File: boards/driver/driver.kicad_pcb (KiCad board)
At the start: 2 copper layers, 228.6 x 116.8 mm, 485 parts, among them Q1 MMBT2907, Q10 MMBT2907, Q11 MMBT2222, Q12 MMBT2907, Q13 MMBT2222, Q14 MMBT2907, Q15 MMBT2222, Q16 MMBT2907, Q17 MMBT2222, Q18 MMBT2907, Q19 MMBT2222, Q2 MMBT2222, Q20 MMBT2907, Q21 MMBT2222, Q22 MMBT2907, Q23 MMBT2222, Q24 MMBT2907, Q25 MMBT2222, Q26 MMBT2907, Q27 MMBT2222, Q28 MMBT2222, Q29 MMBT2222, Q3 MMBT2222, Q30 MMBT2222, Q31 MMBT2222, Q32 MMBT2222, Q33 MMBT2222, Q34 MMBT2222, Q35 MMBT2222, Q36 MMBT2222, Q37 MMBT2222, Q38 MMBT2222, Q39 MMBT2222, Q4 MMBT2907, Q40 MMBT2222, Q41 MMBT2222, Q42 MMBT2222, Q43 MMBT2222, Q44 MMBT2222, Q45 MMBT2222, Q46 MMBT2222, Q47 MMBT2222, Q48 MMBT2222, Q49 MMBT2222, Q5 MMBT2222, Q50 MMBT2222, Q51 MMBT2222, Q52 MMBT2222, Q53 MMBT2222, Q54 MMBT2222, Q55 MMBT2222, Q56 MMBT2222, Q57 MMBT2222, Q58 MMBT2222, Q59 MMBT2222, Q6 MMBT2907, Q60 MMBT2222, Q61 MMBT2907, Q62 MMBT2222, Q63 MMBT2222, Q64 MMBT2907, Q65 MMBT2222, Q66 MMBT2222, Q67 MMBT2907, Q68 MMBT2222, Q69 MMBT2222, Q7 MMBT2222, Q70 MMBT2222, Q71 MMBT2907, Q72 MMBT2222, Q73 MMBT2222, Q74 MMBT2222, Q75 MMBT2907, Q76 MMBT2222, Q77 MMBT2222, Q78 MMBT2222, Q79 MMBT2907, Q8 MMBT2907, Q80 MMBT2222, Q81 MMBT2222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

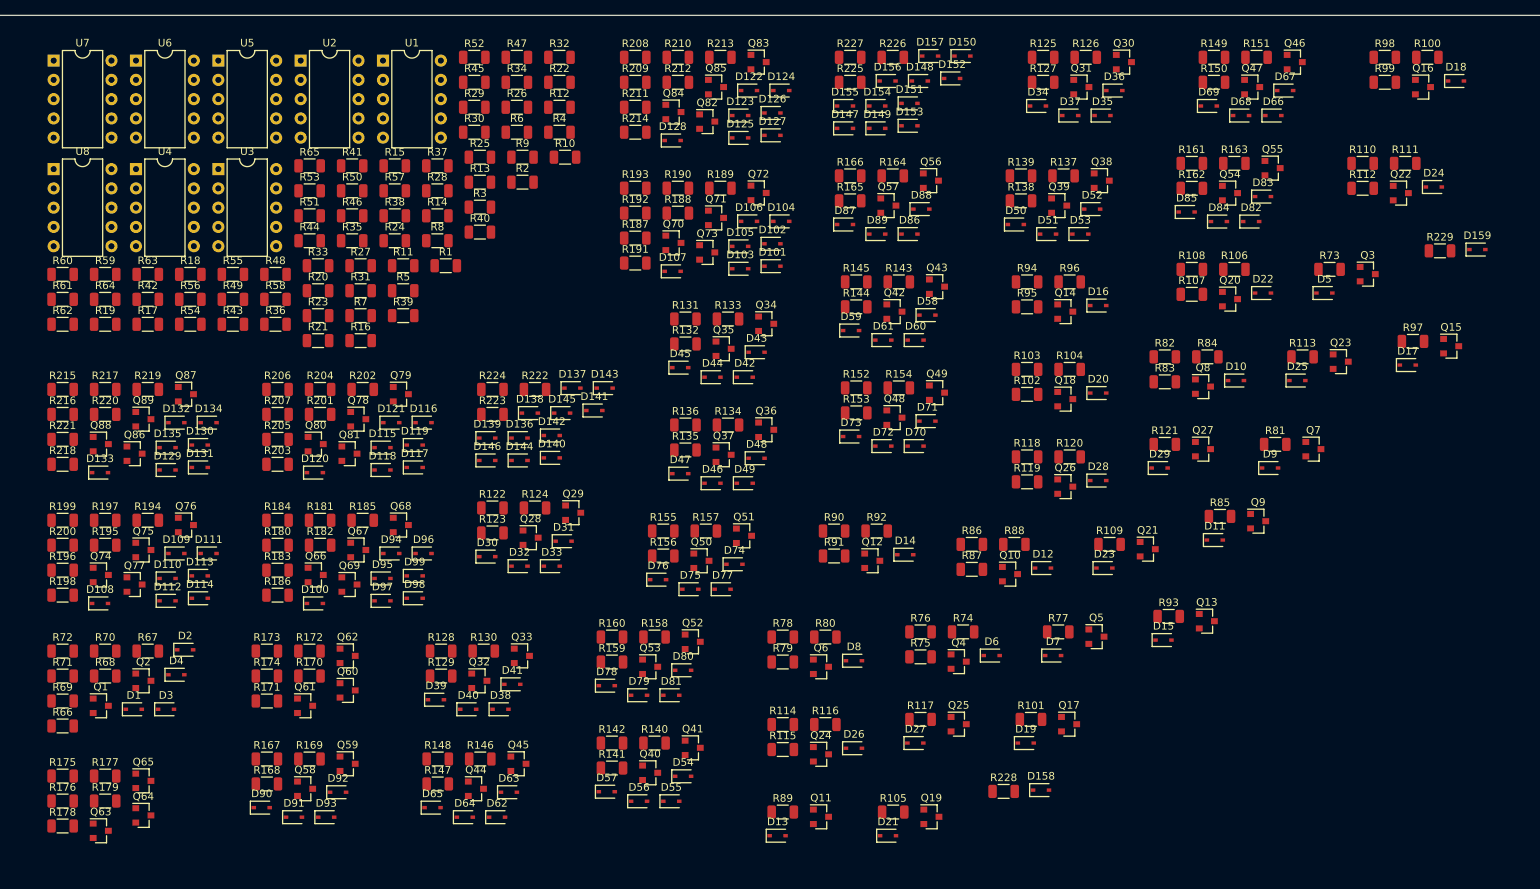
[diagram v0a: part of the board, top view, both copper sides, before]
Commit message: Driver board: a bit more schematic work and some initial footprint selections
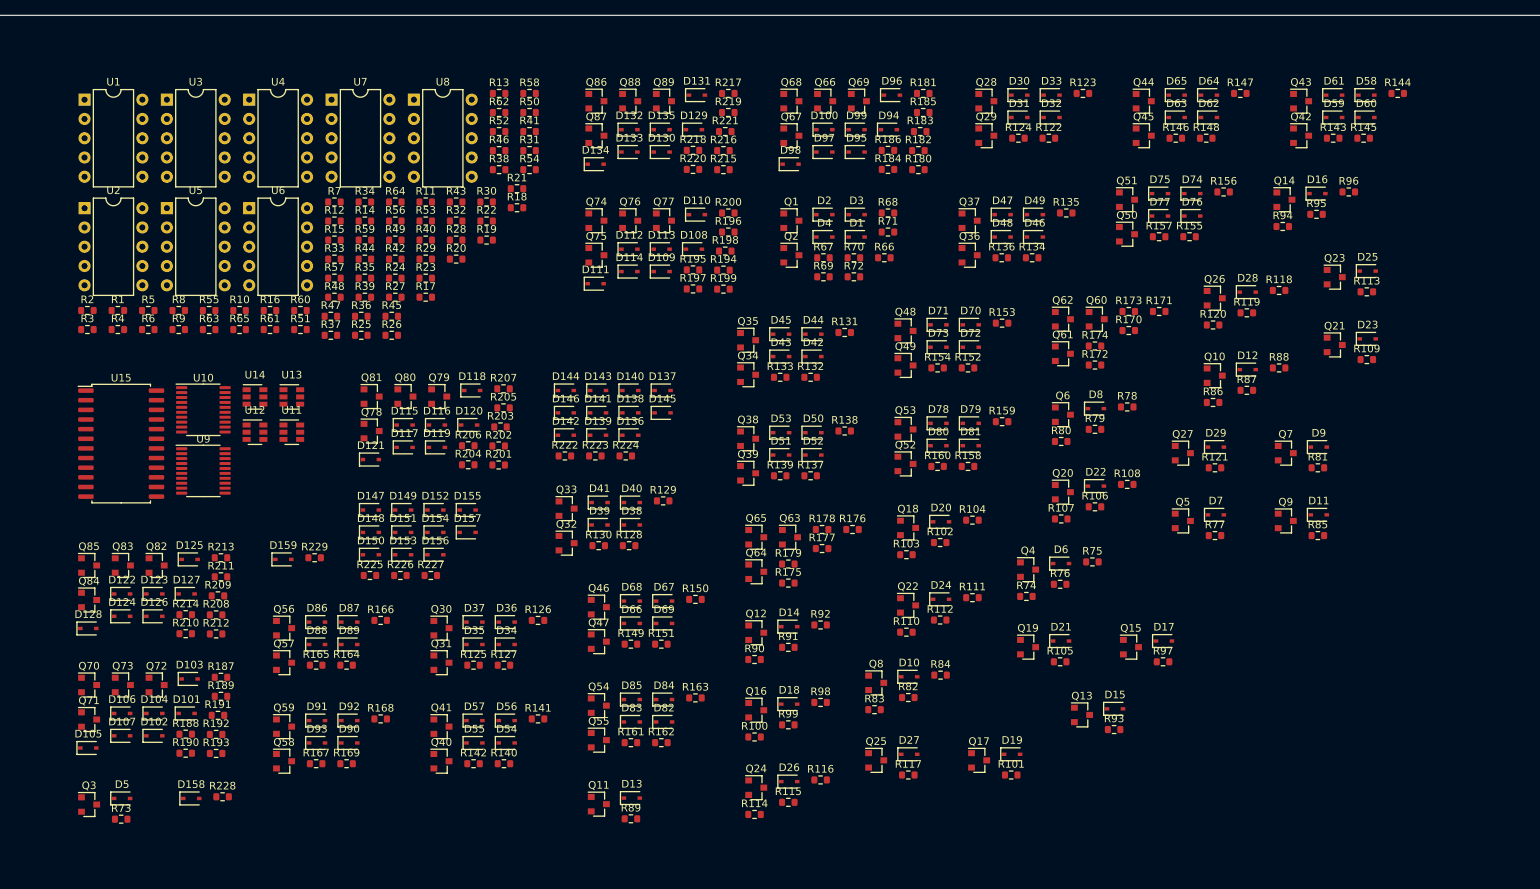
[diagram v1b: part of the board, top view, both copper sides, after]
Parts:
- added U10: 74LVC245, Package_SO:TSSOP-20_4.4x6.5mm_P0.65mm, F.Cu at (71.4, 77.4)
- added U11: 74LVC2G04, Package_TO_SOT_SMD:SOT-23-6, F.Cu at (83.0, 80.3)
- added U12: 74LVC2G04, Package_TO_SOT_SMD:SOT-23-6, F.Cu at (78.2, 80.3)
- added U13: 74LVC2G04, Package_TO_SOT_SMD:SOT-23-6, F.Cu at (83.0, 75.7)
- added U14: 74LVC2G04, Package_TO_SOT_SMD:SOT-23-6, F.Cu at (78.2, 75.7)
- added U15: 74HC4514, Package_SO:SOIC-24W_7.5x15.4mm_P1.27mm, F.Cu at (60.6, 81.8)
- added U9: 74LVC245, Package_SO:TSSOP-20_4.4x6.5mm_P0.65mm, F.Cu at (71.4, 85.4)
- R1, R10, R100, R101, R102, R103, R104, R105, R106, R107, R108, R109, R11, R110, R111, R112, R113, R114, R115, R116, R117, R118, R119, R12, R120, R121, R122, R123, R124, R125, R126, R127, R128, R129, R13, R130, R131, R132, R133, R134, R135, R136, R137, R138, R139, R14, R140, R141, R142, R143, R144, R145, R146, R147, R148, R149, R15, R150, R151, R152, R153, R154, R155, R156, R157, R158, R159, R16, R160, R161, R162, R163, R164, R165, R166, R167, R168, R169, R17, R170, R171, R172, R173, R174, R175, R176, R177, R178, R179, R18, R180, R181, R182, R183, R184, R185, R186, R187, R188, R189, R19, R190, R191, R192, R193, R194, R195, R196, R197, R198, R199, R2, R20, R200, R201, R202, R203, R204, R205, R206, R207, R208, R209, R21, R210, R211, R212, R213, R214, R215, R216, R217, R218, R219, R22, R220, R221, R222, R223, R224, R225, R226, R227, R228, R229, R23, R24, R25, R26, R27, R28, R29, R3, R30, R31, R32, R33, R34, R35, R36, R37, R38, R39, R4, R40, R41, R42, R43, R44, R45, R46, R47, R48, R49, R5, R50, R51, R52, R53, R54, R55, R56, R57, R58, R59, R6, R60, R61, R62, R63, R64, R65, R66, R67, R68, R69, R7, R70, R71, R72, R73, R74, R75, R76, R77, R78, R79, R8, R80, R81, R82, R83, R84, R85, R86, R87, R88, R89, R9, R90, R91, R92, R93, R94, R95, R96, R97, R98, R99: footprint Resistor_SMD:R_1206_3216Metric -> Resistor_SMD:R_0603_1608Metric
- moved Q3 182.4 mm to (56.3, 129.4)
- moved R73 174.9 mm to (60.6, 131.3)
- moved D5 171.9 mm to (60.7, 128.6)
- moved D159 162.6 mm to (81.9, 97.1)
- moved R229 153.7 mm to (86.1, 96.9)
- moved R147 139.5 mm to (208.0, 35.7)
- moved D64 136.6 mm to (203.9, 35.9)
- moved D65 135.8 mm to (199.7, 35.9)
- moved D62 131.5 mm to (203.9, 38.9)
- moved R148 130.2 mm to (203.6, 41.6)
- moved R171 128.3 mm to (197.3, 64.4)
- moved Q44 126.3 mm to (195.3, 36.7)
- moved R100 126.0 mm to (144.0, 120.5)
- moved D63 125.1 mm to (199.7, 38.9)
- moved R66 124.6 mm to (161.1, 57.3)
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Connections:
- R113 pad 2: (no net) -> /FPGA and Power/STEN10
- R117 pad 2: (no net) -> /FPGA and Power/STEN11
- R121 pad 2: (no net) -> /FPGA and Power/STEN12

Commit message: Driver board: finished first rough draft schematic. Lots of placeholders, but at least every place is held.
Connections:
- net /Strand Select/SE01 renamed /Strand Select/SE1
- net /Strand Select/SE02 renamed /Strand Select/SE2
- net /Strand Select/SE03 renamed /Strand Select/SE3
- net /Strand Select/SE04 renamed /Strand Select/SE4
- net /Strand Select/SE05 renamed /Strand Select/SE5
- net /Strand Select/SE06 renamed /Strand Select/SE6
- net /Strand Select/SE07 renamed /Strand Select/SE7
- net /Strand Select/SE08 renamed /Strand Select/SE8
- net /Strand Select/SE09 renamed /Strand Select/SE9
- net /Strand Select/STR01 renamed /Strand Select/STR1
- net /Strand Select/STR02 renamed /Strand Select/STR2
- net /Strand Select/STR03 renamed /Strand Select/STR3
- net /Strand Select/STR04 renamed /Strand Select/STR4
- net /Strand Select/STR05 renamed /Strand Select/STR5
- net /Strand Select/STR06 renamed /Strand Select/STR6
- net /Strand Select/STR07 renamed /Strand Select/STR7
- net /Strand Select/STR08 renamed /Strand Select/STR8
- net /Strand Select/STR09 renamed /Strand Select/STR9
- R101 pad 2: (no net) -> /FPGA and Power/STEN7
- R105 pad 2: (no net) -> /FPGA and Power/STEN8
- R109 pad 2: (no net) -> /FPGA and Power/STEN9
- R122 pad 2: (no net) -> /FPGA and Power/~IL8
- R125 pad 2: (no net) -> /FPGA and Power/~IL7
- R128 pad 2: (no net) -> /FPGA and Power/~IL6
- R131 pad 2: (no net) -> /FPGA and Power/~IL5
- R134 pad 2: (no net) -> /FPGA and Power/~IL4
- R137 pad 2: (no net) -> /FPGA and Power/~IL3
- R140 pad 2: (no net) -> /FPGA and Power/~IL2
- R143 pad 2: (no net) -> /FPGA and Power/~IL1
- R146 pad 2: (no net) -> /FPGA and Power/IL8
- R149 pad 2: (no net) -> /FPGA and Power/IL7
- R152 pad 2: (no net) -> /FPGA and Power/IL6
- R155 pad 2: (no net) -> /FPGA and Power/IL5
- R158 pad 2: (no net) -> /FPGA and Power/IL4
- R161 pad 2: (no net) -> /FPGA and Power/IL3
- R164 pad 2: (no net) -> /FPGA and Power/IL2
- R167 pad 2: (no net) -> /FPGA and Power/IL1
- R77 pad 2: (no net) -> /FPGA and Power/STEN1
- R81 pad 2: (no net) -> /FPGA and Power/STEN2
- R85 pad 2: (no net) -> /FPGA and Power/STEN3
- R89 pad 2: (no net) -> /FPGA and Power/STEN4
- R93 pad 2: (no net) -> /FPGA and Power/STEN5
- R97 pad 2: (no net) -> /FPGA and Power/STEN6
- U11 pad 1: (no net) -> /FPGA and Power/IL1
- U11 pad 3: (no net) -> /FPGA and Power/IL2
- U11 pad 4: (no net) -> /FPGA and Power/~IL2
- U11 pad 6: (no net) -> /FPGA and Power/~IL1
- U12 pad 1: (no net) -> /FPGA and Power/IL3
- U12 pad 3: (no net) -> /FPGA and Power/IL4
- U12 pad 4: (no net) -> /FPGA and Power/~IL4
- U12 pad 6: (no net) -> /FPGA and Power/~IL3
- U13 pad 1: (no net) -> /FPGA and Power/IL5
- U13 pad 3: (no net) -> /FPGA and Power/IL6
- U13 pad 4: (no net) -> /FPGA and Power/~IL6
- U13 pad 6: (no net) -> /FPGA and Power/~IL5
- U14 pad 1: (no net) -> /FPGA and Power/IL7
- U14 pad 3: (no net) -> /FPGA and Power/IL8
- U14 pad 4: (no net) -> /FPGA and Power/~IL8
- U14 pad 6: (no net) -> /FPGA and Power/~IL7
- U15 pad 10: (no net) -> /FPGA and Power/STEN2
- U15 pad 17: (no net) -> /FPGA and Power/STEN9
- U15 pad 18: (no net) -> /FPGA and Power/STEN8
- U15 pad 4: (no net) -> /FPGA and Power/STEN7
- U15 pad 5: (no net) -> /FPGA and Power/STEN6
- U15 pad 6: (no net) -> /FPGA and Power/STEN5
- U15 pad 7: (no net) -> /FPGA and Power/STEN4
- U15 pad 8: (no net) -> /FPGA and Power/STEN3
- U15 pad 9: (no net) -> /FPGA and Power/STEN1

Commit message: Driver board: significant cleanup. Moved sense amp pairs into a subsheet, split tuning resistors into two globally, pushed input circuits into their corresponding sheets.
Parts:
- removed R1, R2: 2.7k, Resistor_SMD:R_0603_1608Metric
- removed U1: SN7524, Package_DIP:DIP-10_W7.62mm
- added C10: 0.1uF, Capacitor_SMD:C_0603_1608Metric, F.Cu at (99.2, 89.6)
- added C11: 0.1uF, Capacitor_SMD:C_0603_1608Metric, F.Cu at (95.2, 94.6)
- added C12: 10nF, Capacitor_SMD:C_0603_1608Metric, F.Cu at (170.0, 43.5)
- added C13: 100pF, Capacitor_SMD:C_0603_1608Metric, F.Cu at (147.3, 64.6)
- added C14: 0.1uF, Capacitor_SMD:C_0603_1608Metric, F.Cu at (166.0, 43.5)
- added C15: 0.1uF, Capacitor_SMD:C_0603_1608Metric, F.Cu at (162.0, 46.0)
- added C16: 10nF, Capacitor_SMD:C_0603_1608Metric, F.Cu at (97.0, 117.4)
- added C17: 100pF, Capacitor_SMD:C_0603_1608Metric, F.Cu at (78.3, 136.0)
- added C18: 0.1uF, Capacitor_SMD:C_0603_1608Metric, F.Cu at (89.0, 124.9)
- added C19: 0.1uF, Capacitor_SMD:C_0603_1608Metric, F.Cu at (93.0, 119.9)
- added C20: 10nF, Capacitor_SMD:C_0603_1608Metric, F.Cu at (51.6, 144.2)
- added C21: 100pF, Capacitor_SMD:C_0603_1608Metric, F.Cu at (47.6, 146.7)
- added C22: 0.1uF, Capacitor_SMD:C_0603_1608Metric, F.Cu at (43.6, 151.8)
- added C23: 0.1uF, Capacitor_SMD:C_0603_1608Metric, F.Cu at (33.0, 162.8)
- added C24: 10nF, Capacitor_SMD:C_0603_1608Metric, F.Cu at (215.4, 19.1)
- added C25: 100pF, Capacitor_SMD:C_0603_1608Metric, F.Cu at (211.3, 21.7)
- added C26: 0.1uF, Capacitor_SMD:C_0603_1608Metric, F.Cu at (207.3, 26.7)
- added C27: 0.1uF, Capacitor_SMD:C_0603_1608Metric, F.Cu at (192.7, 37.7)
- added C28: 10nF, Capacitor_SMD:C_0603_1608Metric, F.Cu at (140.6, 94.6)
- added C29: 100pF, Capacitor_SMD:C_0603_1608Metric, F.Cu at (140.6, 87.1)
- added C3: 6.8uF, Capacitor_Tantalum_SMD:CP_EIA-7343-31_Kemet-D, F.Cu at (208.3, 94.6)
- added C30: 0.1uF, Capacitor_SMD:C_0603_1608Metric, F.Cu at (140.6, 89.6)
- added C31: 0.1uF, Capacitor_SMD:C_0603_1608Metric, F.Cu at (140.6, 84.6)
- added C32: 10nF, Capacitor_SMD:C_0603_1608Metric, F.Cu at (162.0, 16.6)
- added C33: 100pF, Capacitor_SMD:C_0603_1608Metric, F.Cu at (147.3, 37.7)
- added C34: 0.1uF, Capacitor_SMD:C_0603_1608Metric, F.Cu at (166.0, 16.6)
- added C35: 0.1uF, Capacitor_SMD:C_0603_1608Metric, F.Cu at (162.0, 19.1)
- added C36: 6.8uF, Capacitor_Tantalum_SMD:CP_EIA-7343-31_Kemet-D, F.Cu at (186.4, 108.2)
- added C37: 6.8uF, Capacitor_Tantalum_SMD:CP_EIA-7343-31_Kemet-D, F.Cu at (206.4, 108.2)
- added C38: 6.8uF, Capacitor_Tantalum_SMD:CP_EIA-7343-31_Kemet-D, F.Cu at (259.2, 31.9)
- added C39: 6.8uF, Capacitor_Tantalum_SMD:CP_EIA-7343-31_Kemet-D, F.Cu at (162.3, 140.3)
- added C4: 10nF, Capacitor_SMD:C_0603_1608Metric, F.Cu at (47.6, 114.9)
- added C40: 6.8uF, Capacitor_Tantalum_SMD:CP_EIA-7343-31_Kemet-D, F.Cu at (160.7, 153.9)
- added C41: 6.8uF, Capacitor_Tantalum_SMD:CP_EIA-7343-31_Kemet-D, F.Cu at (230.1, 76.1)
- added C42: 6.8uF, Capacitor_Tantalum_SMD:CP_EIA-7343-31_Kemet-D, F.Cu at (184.2, 120.8)
- added C43: 6.8uF, Capacitor_Tantalum_SMD:CP_EIA-7343-31_Kemet-D, F.Cu at (259.2, 44.5)
- added C44: 6.8uF, Capacitor_Tantalum_SMD:CP_EIA-7343-31_Kemet-D, F.Cu at (235.3, 63.5)
- added C45: 1.0uF, Capacitor_Tantalum_SMD:CP_EIA-3216-18_Kemet-A, F.Cu at (158.3, 70.6)
- added C46: 1.0uF, Capacitor_Tantalum_SMD:CP_EIA-3216-18_Kemet-A, F.Cu at (63.4, 160.0)
- added C47: 0.1uF, Capacitor_SMD:C_0603_1608Metric, F.Cu at (41.0, 50.1)
- added C48: 0.1uF, Capacitor_SMD:C_0603_1608Metric, F.Cu at (30.4, 64.8)
- added C49: 0.33uF, Capacitor_SMD:C_0603_1608Metric, F.Cu at (26.4, 64.8)
- added C5: 100pF, Capacitor_SMD:C_0603_1608Metric, F.Cu at (43.6, 117.4)
- added C50: 10nF, Capacitor_SMD:C_0603_1608Metric, F.Cu at (34.4, 62.3)
- added C51: 0.1uF, Capacitor_SMD:C_0603_1608Metric, F.Cu at (34.4, 59.8)
- added C52: 0.1uF, Capacitor_SMD:C_0603_1608Metric, F.Cu at (26.4, 59.8)
- added C53: 0.1uF, Capacitor_SMD:C_0603_1608Metric, F.Cu at (41.0, 52.6)
- added C54: 0.1uF, Capacitor_SMD:C_0603_1608Metric, F.Cu at (26.4, 67.3)
- added C55: 0.1uF, Capacitor_SMD:C_0603_1608Metric, F.Cu at (30.4, 59.8)
- added C6: 0.1uF, Capacitor_SMD:C_0603_1608Metric, F.Cu at (29.0, 136.0)
- added C7: 0.1uF, Capacitor_SMD:C_0603_1608Metric, F.Cu at (43.6, 114.9)
- added C8: 10nF, Capacitor_SMD:C_0603_1608Metric, F.Cu at (84.6, 105.7)
- added C9: 100pF, Capacitor_SMD:C_0603_1608Metric, F.Cu at (103.2, 87.1)
- added J1: Barrel_Jack_Switch, Connector_BarrelJack:BarrelJack_Horizontal, F.Cu at (68.2, 20.7)
- added J2: Conn_01x24, Connector_PinSocket_2.54mm:PinSocket_1x24_P2.54mm_Vertical, F.Cu at (17.5, 17.7)
- added J3: Conn_02x06_Top_Bottom, Connector_PinSocket_2.54mm:PinSocket_2x06_P2.54mm_Vertical, F.Cu at (51.3, 17.7)
- added J4: Conn_01x24, Connector_PinSocket_2.54mm:PinSocket_1x24_P2.54mm_Vertical, F.Cu at (22.1, 17.7)
- added J5: Conn_01x24, Connector_PinHeader_1.00mm:PinHeader_1x24_P1.00mm_Vertical, F.Cu at (16.9, 84.8)
- added J6: Conn_01x24, Connector_PinHeader_1.00mm:PinHeader_1x24_P1.00mm_Vertical, F.Cu at (20.2, 84.8)
- added J7: Conn_01x24, Connector_PinHeader_1.00mm:PinHeader_1x24_P1.00mm_Vertical, F.Cu at (23.6, 84.8)
- added J8: Conn_01x24, Connector_PinHeader_1.00mm:PinHeader_1x24_P1.00mm_Vertical, F.Cu at (26.9, 84.8)
- added L1: 8.2uH, Inductor_SMD:L_1812_4532Metric, F.Cu at (216.7, 94.2)
- added L10: 2.2uH, Inductor_SMD:L_1812_4532Metric, F.Cu at (235.9, 35.8)
- added L11: 2.2uH, Inductor_SMD:L_1812_4532Metric, F.Cu at (184.9, 80.6)
- added L12: 2.2uH, Inductor_SMD:L_1812_4532Metric, F.Cu at (212.0, 59.4)
- added L13: 2.2uH, Inductor_SMD:L_1812_4532Metric, F.Cu at (138.9, 126.2)
- added L14: 2.2uH, Inductor_SMD:L_1812_4532Metric, F.Cu at (160.8, 112.6)
- added L15: 2.2uH, Inductor_SMD:L_1812_4532Metric, F.Cu at (115.5, 148.5)
- added L16: 2.2uH, Inductor_SMD:L_1812_4532Metric, F.Cu at (257.3, 17.9)
- added L17: 2.2uH, Inductor_SMD:L_1812_4532Metric, F.Cu at (93.6, 148.5)
- added L18: 2.2uH, Inductor_SMD:L_1812_4532Metric, F.Cu at (138.9, 112.6)
- added L19: 3.9uH, Inductor_SMD:L_1812_4532Metric, F.Cu at (64.0, 142.9)
- added L2: 8.2uH, Inductor_SMD:L_1812_4532Metric, F.Cu at (194.8, 107.8)
- added L20: 3.9uH, Inductor_SMD:L_1812_4532Metric, F.Cu at (64.0, 147.9)
- added L21: 3.9uH, Inductor_SMD:L_1812_4532Metric, F.Cu at (182.4, 49.6)
- added L22: 3.9uH, Inductor_SMD:L_1812_4532Metric, F.Cu at (182.4, 44.7)
- added L23: 3.9uH, Inductor_SMD:L_1812_4532Metric, F.Cu at (109.4, 112.6)
- added L24: 3.9uH, Inductor_SMD:L_1812_4532Metric, F.Cu at (109.4, 117.5)
- added L25: 3.9uH, Inductor_SMD:L_1812_4532Metric, F.Cu at (227.7, 17.9)
- added L26: 3.9uH, Inductor_SMD:L_1812_4532Metric, F.Cu at (227.7, 22.8)
- added L27: 3.9uH, Inductor_SMD:L_1812_4532Metric, F.Cu at (109.4, 130.5)
- added L28: 3.9uH, Inductor_SMD:L_1812_4532Metric, F.Cu at (109.4, 135.5)
- added L29: 3.9uH, Inductor_SMD:L_1812_4532Metric, F.Cu at (182.4, 62.6)
- added L3: 2.2uH, Inductor_SMD:L_1812_4532Metric, F.Cu at (184.9, 94.2)
- added L30: 3.9uH, Inductor_SMD:L_1812_4532Metric, F.Cu at (182.4, 67.6)
- added L31: 8.2uH, Inductor_SMD:L_1812_4532Metric, F.Cu at (214.8, 107.8)
- added L32: 8.2uH, Inductor_SMD:L_1812_4532Metric, F.Cu at (267.6, 31.5)
- added L33: 8.2uH, Inductor_SMD:L_1812_4532Metric, F.Cu at (170.7, 139.8)
- added L34: 8.2uH, Inductor_SMD:L_1812_4532Metric, F.Cu at (169.1, 153.4)
- added L35: 8.2uH, Inductor_SMD:L_1812_4532Metric, F.Cu at (238.5, 75.6)
- added L36: 8.2uH, Inductor_SMD:L_1812_4532Metric, F.Cu at (192.6, 120.4)
- added L37: 8.2uH, Inductor_SMD:L_1812_4532Metric, F.Cu at (267.6, 44.1)
- added L38: 8.2uH, Inductor_SMD:L_1812_4532Metric, F.Cu at (243.7, 63.0)
- added L4: 2.2uH, Inductor_SMD:L_1812_4532Metric, F.Cu at (137.3, 153.4)
- added L5: 2.2uH, Inductor_SMD:L_1812_4532Metric, F.Cu at (160.8, 126.2)
- added L6: 2.2uH, Inductor_SMD:L_1812_4532Metric, F.Cu at (206.8, 80.6)
- added L7: 2.2uH, Inductor_SMD:L_1812_4532Metric, F.Cu at (235.9, 49.4)
- added L8: 2.2uH, Inductor_SMD:L_1812_4532Metric, F.Cu at (138.9, 139.8)
- added L9: 2.2uH, Inductor_SMD:L_1812_4532Metric, F.Cu at (137.1, 71.5)
- added Q90: IRF7413, Package_SO:SO-8_3.9x4.9mm_P1.27mm, F.Cu at (59.5, 39.3)
- added R230: NOM, Resistor_SMD:R_0603_1608Metric, F.Cu at (247.5, 24.6)
- added R231: 7.5, Resistor_SMD:R_0603_1608Metric, F.Cu at (235.0, 28.7)
- added R232: NOM, Resistor_SMD:R_0603_1608Metric, F.Cu at (246.4, 19.6)
- added R233: 1k, Resistor_SMD:R_0603_1608Metric, F.Cu at (116.6, 141.4)
- added R234: 1k, Resistor_SMD:R_0603_1608Metric, F.Cu at (128.0, 132.3)
- added R235: 5.1k, Resistor_SMD:R_0603_1608Metric, F.Cu at (128.9, 140.2)
- added R236: 5.1k, Resistor_SMD:R_0603_1608Metric, F.Cu at (129.1, 137.3)
- added R237: 27, Resistor_SMD:R_0603_1608Metric, F.Cu at (124.9, 140.2)
- added R238: 7.5, Resistor_SMD:R_0603_1608Metric, F.Cu at (129.1, 134.8)
- added R239: NOM, Resistor_SMD:R_0603_1608Metric, F.Cu at (125.1, 137.7)
- added R240: 7.5, Resistor_SMD:R_0603_1608Metric, F.Cu at (125.1, 135.2)
- added R241: NOM, Resistor_SMD:R_0603_1608Metric, F.Cu at (120.9, 139.8)
- added R242: 1k, Resistor_SMD:R_0603_1608Metric, F.Cu at (198.1, 67.3)
- added R243: 1k, Resistor_SMD:R_0603_1608Metric, F.Cu at (198.1, 69.8)
- added R244: 5.1k, Resistor_SMD:R_0603_1608Metric, F.Cu at (202.1, 66.9)
- added R245: 5.1k, Resistor_SMD:R_0603_1608Metric, F.Cu at (202.1, 69.4)
- added R246: 27, Resistor_SMD:R_0603_1608Metric, F.Cu at (201.9, 72.3)
- added R247: 7.5, Resistor_SMD:R_0603_1608Metric, F.Cu at (189.6, 73.4)
- added R248: NOM, Resistor_SMD:R_0603_1608Metric, F.Cu at (197.9, 72.3)
- added R249: 7.5, Resistor_SMD:R_0603_1608Metric, F.Cu at (193.9, 71.8)
- added R250: NOM, Resistor_SMD:R_0603_1608Metric, F.Cu at (201.0, 64.3)
- added R251: 200, Resistor_SMD:R_0603_1608Metric, F.Cu at (210.5, 52.3)
- added R252: 200, Resistor_SMD:R_0603_1608Metric, F.Cu at (214.5, 52.3)
- added R253: 200, Resistor_SMD:R_0603_1608Metric, F.Cu at (218.5, 52.3)
- added R254: 200, Resistor_SMD:R_0603_1608Metric, F.Cu at (159.5, 103.0)
- added R255: 200, Resistor_SMD:R_0603_1608Metric, F.Cu at (163.5, 103.0)
- added R256: 200, Resistor_SMD:R_0603_1608Metric, F.Cu at (167.5, 103.0)
- added R257: 3k, Resistor_SMD:R_0603_1608Metric, F.Cu at (157.5, 73.4)
- added R258: 3k, Resistor_SMD:R_0603_1608Metric, F.Cu at (62.6, 162.8)
- added R259: 1020k, Resistor_SMD:R_0603_1608Metric, F.Cu at (26.4, 55.1)
- added R260: 2.87k, Resistor_SMD:R_0603_1608Metric, F.Cu at (30.4, 54.8)
- added R261: 9.76k, Resistor_SMD:R_0603_1608Metric, F.Cu at (34.4, 54.8)
- added R262: 54.9k, Resistor_SMD:R_0603_1608Metric, F.Cu at (30.4, 57.3)
- added R263: 0.025, Resistor_SMD:R_0603_1608Metric, F.Cu at (34.4, 57.3)
- added R264: 10, Resistor_SMD:R_0603_1608Metric, F.Cu at (38.5, 55.1)
- added R265: 1k, Resistor_SMD:R_0603_1608Metric, F.Cu at (38.5, 57.7)
- added R266: 10k, Resistor_SMD:R_0603_1608Metric, F.Cu at (26.4, 62.3)
- added R267: 10k, Resistor_SMD:R_0603_1608Metric, F.Cu at (30.4, 62.3)
- added T1: 1:1, lachesis:Transformer_Murata_786J, F.Cu at (34.3, 129.5)
- added T10: 1:1, lachesis:Transformer_Murata_786J, F.Cu at (34.3, 145.7)
- added T11: 1:1, lachesis:Transformer_Murata_786J, F.Cu at (198.0, 20.7)
- added T12: 1:1, lachesis:Transformer_Murata_786J, F.Cu at (198.0, 31.2)
- added T13: 1:1, lachesis:Transformer_Murata_786J, F.Cu at (131.2, 99.1)
- added T14: 1:1, lachesis:Transformer_Murata_786J, F.Cu at (131.2, 88.6)
- added T15: 1:1, lachesis:Transformer_Murata_786J, F.Cu at (152.7, 31.2)
- added T16: 1:1, lachesis:Transformer_Murata_786J, F.Cu at (152.7, 20.7)
- added T2: 1:1, lachesis:Transformer_Murata_786J, F.Cu at (34.3, 118.9)
- added T3: 1:1, lachesis:Transformer_Murata_786J, F.Cu at (85.9, 99.1)
- added T4: 1:1, lachesis:Transformer_Murata_786J, F.Cu at (85.9, 88.6)
- added T5: 1:1, lachesis:Transformer_Murata_786J, F.Cu at (152.7, 47.5)
- added T6: 1:1, lachesis:Transformer_Murata_786J, F.Cu at (152.7, 58.0)
- added T7: 1:1, lachesis:Transformer_Murata_786J, F.Cu at (79.6, 118.9)
- added T8: 1:1, lachesis:Transformer_Murata_786J, F.Cu at (79.6, 129.5)
- added T9: 1:1, lachesis:Transformer_Murata_786J, F.Cu at (34.3, 156.3)
- added U16: 74LVC2G04, Package_TO_SOT_SMD:SOT-23-6, F.Cu at (31.7, 51.2)
- added U17: 74LVC2G04, Package_TO_SOT_SMD:SOT-23-6, F.Cu at (26.8, 51.2)
- added U18: 74LVC2G04, Package_TO_SOT_SMD:SOT-23-6, F.Cu at (36.5, 51.2)
- Q1, Q10, Q12, Q14, Q16, Q18, Q20, Q22, Q24, Q26, Q4, Q6, Q8: value MMBT2907 -> MMBT2222
- Q11, Q13, Q15, Q17, Q19, Q2, Q21, Q23, Q25, Q27, Q5, Q7, Q9: value MMBT2222 -> MMBT2907
- R10, R15, R16, R33, R34, R39, R40, R41, R42, R47, R48, R7, R8, R9: value 2.7k -> 470
- R100, R104, R108, R112, R116, R120, R76, R80, R84, R88, R92, R96: value 3k -> 5.1k
- R101, R105, R109, R113, R117, R121, R194, R77, R81, R85, R89, R93, R97: value 500 -> 2k
- R102, R106, R110, R114, R118, R78, R82, R86, R90, R94, R98: value 5.1k -> 3k
- R103, R107, R111, R115, R119, R179, R75, R79, R83, R87, R91, R95, R99: value 2k -> 1k
- R122: value 500 -> 3k
- R123, R135, R147, R159: value 390 -> 1k
- R124, R136, R148, R160: value NOM -> 390
- R125, R137, R149, R161: value 500 -> 3.9
- R126, R138, R150, R162: value 390 -> NOM
- R127, R139, R151, R163, R192, R206, R207: value NOM -> 1k
- R128, R140, R152, R164, R180: value 500 -> 390
- R129, R141, R153, R165: value 390 -> 3.9
- R131, R143, R155, R167, R187, R215: value 500 -> 1k
- R133, R145, R157, R169, R185: value NOM -> 3.9
- R134, R146, R158: value 500 -> NOM
- R170: value 1k -> NOM
- R171: value 470 -> 1k
- R172: value 2k -> 390
- R173: value 750 -> 3.9
- R174: value 2k -> NOM
- R176: value 470 -> 390
- R177: value 2k -> 3.9
- R178: value 750 -> NOM
- R181: value 1k -> 3.9
- R182, R203, R74: value 5.1k -> NOM
- R183, R197, R67: value 5.1k -> 1k
- R184: value 27 -> 390
- R188: value 1k -> 470
- R189, R196: value 5.1k -> 2k
- R19, R20, R21, R22, R27, R28, R29, R30, R51, R52, R53, R54, R59, R60, R61, R62: value 470 -> 2.7k
- R190: value 5.1k -> 750
- R191: value 27 -> 2k
- R193: value NOM -> 470
- R195: value 1k -> 750
- R198: value 27 -> 1k
- R199, R200, R71: value NOM -> 5.1k
- R201: value 500 -> 27
- R202: value 1k -> 7.5
- R204, R211: value 5.1k -> 7.5
- R205, R212: value 27 -> NOM
- R208: value 500 -> 5.1k
- R209: value 1k -> 5.1k
- R210: value 5.1k -> 27
- R213, R220: value NOM -> 7.5
- R222: value 200 -> 7.5
- R223: value 200 -> NOM
- R224, R225: value 200 -> 1k
- R226, R227: value 200 -> 5.1k
- R228: value 3k -> 27
- R229: value 3k -> 7.5
- R65: value 5k -> 470
- R66: value 5.1k -> 470
- R68: value 680 -> 5.1k
- R70: value 3k -> 680
- R72: value 6 -> 3k
- R73: value 500 -> 8.2
- U11: value 74LVC2G04 -> 74LVC245; footprint Package_TO_SOT_SMD:SOT-23-6 -> Package_SO:TSSOP-20_4.4x6.5mm_P0.65mm
- U12: value 74LVC2G04 -> JTE0624D05; footprint Package_TO_SOT_SMD:SOT-23-6 -> Converter_DCDC:Converter_DCDC_XP_POWER_JTExxxxDxx_THT
- U13: value 74LVC2G04 -> LTC4231-1; footprint Package_TO_SOT_SMD:SOT-23-6 -> Package_SO:MSOP-12_3x4mm_P0.65mm
- U14: value 74LVC2G04 -> 74HC4514; footprint Package_TO_SOT_SMD:SOT-23-6 -> Package_SO:SOIC-24W_7.5x15.4mm_P1.27mm
- U15: value 74HC4514 -> 74LVC2G04; footprint Package_SO:SOIC-24W_7.5x15.4mm_P1.27mm -> Package_TO_SOT_SMD:SOT-23-6
- U2, U3, U4, U5, U6, U7, U8: footprint Package_DIP:DIP-10_W7.62mm -> Package_DIP:DIP-16_W7.62mm_Socket
- U9: value 74LVC245 -> SN7524; footprint Package_SO:TSSOP-20_4.4x6.5mm_P0.65mm -> Package_DIP:DIP-16_W7.62mm_Socket
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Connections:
- D1 pad 1: Net-(D1-Pad1) -> GND
- D1 pad 2: /Strand Select/BPLSWZ -> Net-(D1-Pad2)
- D10 pad 1: Net-(D10-Pad1) -> GND
- D10 pad 2: /Strand Select/BPLSWZ -> Net-(D10-Pad2)
- D11 pad 1: GND -> Net-(D11-Pad1)
- D11 pad 2: Net-(D11-Pad2) -> /Strand Select/BPLSWZ
- D12 pad 1: Net-(D12-Pad1) -> GND
- D12 pad 2: /Strand Select/BPLSWZ -> Net-(D12-Pad2)
- D13 pad 1: GND -> Net-(D13-Pad1)
- D13 pad 2: Net-(D13-Pad2) -> /Strand Select/BPLSWZ
- D136 pad 1: (no net) -> /Connector/RFD1
- D137 pad 1: (no net) -> /Connector/RFD3
- D138 pad 1: /Rope Drivers/RSTRD4 -> /Connector/RSTRD4
- D139 pad 1: (no net) -> /Connector/RCD1
- D14 pad 1: Net-(D14-Pad1) -> GND
- D14 pad 2: /Strand Select/BPLSWZ -> Net-(D14-Pad2)
- D140 pad 1: (no net) -> /Connector/RCD3
- D141 pad 1: (no net) -> /Connector/RFD2
- D142 pad 1: (no net) -> /Connector/RFD4
- D143 pad 1: /Rope Drivers/RSTRD3 -> /Connector/RSTRD3
- D144 pad 1: (no net) -> /Connector/RCD2
- D145 pad 1: (no net) -> /Connector/RCD4
- D146 pad 1: /Rope Drivers/SETRN1 -> /Connector/SETRN1
- D147 pad 1: (no net) -> /Connector/RFD5
- D148 pad 1: (no net) -> /Connector/RFD7
- D149 pad 1: /Rope Drivers/RSTRD2 -> /Connector/RSTRD2
- D15 pad 1: GND -> Net-(D15-Pad1)
- D15 pad 2: Net-(D15-Pad2) -> /Strand Select/BPLSWZ
- D150 pad 1: (no net) -> /Connector/RCD5
- D151 pad 1: (no net) -> /Connector/RCD7
- D152 pad 1: (no net) -> /Connector/RFD6
- D153 pad 1: (no net) -> /Connector/RFD8
- D154 pad 1: /Rope Drivers/RSTRD1 -> /Connector/RSTRD1
- D155 pad 1: (no net) -> /Connector/RCD6
- D156 pad 1: (no net) -> /Connector/RCD8
- D157 pad 1: /Rope Drivers/SETRN2 -> /Connector/SETRN2
- D16 pad 1: Net-(D16-Pad1) -> GND
- D16 pad 2: /Strand Select/BPLSWZ -> Net-(D16-Pad2)
- D17 pad 1: GND -> Net-(D17-Pad1)
- D17 pad 2: Net-(D17-Pad2) -> /Strand Select/BPLSWZ
- D18 pad 1: Net-(D18-Pad1) -> GND
- D18 pad 2: /Strand Select/BPLSWZ -> Net-(D18-Pad2)
- D19 pad 1: GND -> Net-(D19-Pad1)
- D19 pad 2: Net-(D19-Pad2) -> /Strand Select/BPLSWZ
- D2 pad 2: Net-(D2-Pad2) -> /Strand Select/BPLSWZ
- D20 pad 1: Net-(D20-Pad1) -> GND
- D20 pad 2: /Strand Select/BPLSWZ -> Net-(D20-Pad2)
- D21 pad 1: GND -> Net-(D21-Pad1)
- D21 pad 2: Net-(D21-Pad2) -> /Strand Select/BPLSWZ
- D22 pad 1: Net-(D22-Pad1) -> GND
- D22 pad 2: /Strand Select/BPLSWZ -> Net-(D22-Pad2)
- D23 pad 1: GND -> Net-(D23-Pad1)
- D23 pad 2: Net-(D23-Pad2) -> /Strand Select/BPLSWZ
- D24 pad 1: Net-(D24-Pad1) -> GND
- D24 pad 2: /Strand Select/BPLSWZ -> Net-(D24-Pad2)
- D25 pad 1: GND -> Net-(D25-Pad1)
- D25 pad 2: Net-(D25-Pad2) -> /Strand Select/BPLSWZ
- D26 pad 1: Net-(D26-Pad1) -> GND
- D26 pad 2: /Strand Select/BPLSWZ -> Net-(D26-Pad2)
- D27 pad 1: GND -> Net-(D27-Pad1)
- D27 pad 2: Net-(D27-Pad2) -> /Strand Select/BPLSWZ
- D28 pad 1: Net-(D28-Pad1) -> GND
- D28 pad 2: /Strand Select/BPLSWZ -> Net-(D28-Pad2)
- D29 pad 1: GND -> Net-(D29-Pad1)
- D29 pad 2: Net-(D29-Pad2) -> /Strand Select/BPLSWZ
- D3 pad 2: Net-(D2-Pad1) -> Net-(D3-Pad2)
- D5 pad 2: Net-(D5-Pad2) -> Net-(D4-Pad1)
- D6 pad 1: Net-(D6-Pad1) -> GND
- D6 pad 2: /Strand Select/BPLSWZ -> Net-(D6-Pad2)
- D7 pad 1: GND -> Net-(D7-Pad1)
- D7 pad 2: Net-(D7-Pad2) -> /Strand Select/BPLSWZ
- D8 pad 1: Net-(D8-Pad1) -> GND
- D8 pad 2: /Strand Select/BPLSWZ -> Net-(D8-Pad2)
- D9 pad 1: GND -> Net-(D9-Pad1)
- D9 pad 2: Net-(D9-Pad2) -> /Strand Select/BPLSWZ
- Q1 pad 2: Net-(D1-Pad1) -> Net-(D1-Pad2)
- Q1 pad 3: Net-(Q1-Pad3) -> /Strand Select/RPR
- Q10 pad 2: Net-(D12-Pad1) -> Net-(D12-Pad2)
- Q10 pad 3: /Strand Select/STR4 -> Net-(Q10-Pad3)
- Q11 pad 2: Net-(D13-Pad2) -> Net-(D13-Pad1)
- Q11 pad 3: /Strand Select/SE4 -> /Connector/STR4
- Q12 pad 2: Net-(D14-Pad1) -> Net-(D14-Pad2)
- Q12 pad 3: /Strand Select/STR5 -> Net-(Q12-Pad3)
- Q13 pad 2: Net-(D15-Pad2) -> Net-(D15-Pad1)
- Q13 pad 3: /Strand Select/SE5 -> /Connector/STR5
- Q14 pad 2: Net-(D16-Pad1) -> Net-(D16-Pad2)
- Q14 pad 3: /Strand Select/STR6 -> Net-(Q14-Pad3)
- Q15 pad 2: Net-(D17-Pad2) -> Net-(D17-Pad1)
- Q15 pad 3: /Strand Select/SE6 -> /Connector/STR6
- Q16 pad 2: Net-(D18-Pad1) -> Net-(D18-Pad2)
- Q16 pad 3: /Strand Select/STR7 -> Net-(Q16-Pad3)
- Q17 pad 2: Net-(D19-Pad2) -> Net-(D19-Pad1)
- Q17 pad 3: /Strand Select/SE7 -> /Connector/STR7
- Q18 pad 2: Net-(D20-Pad1) -> Net-(D20-Pad2)
- Q18 pad 3: /Strand Select/STR8 -> Net-(Q18-Pad3)
- Q19 pad 2: Net-(D21-Pad2) -> Net-(D21-Pad1)
- Q19 pad 3: /Strand Select/SE8 -> /Connector/STR8
- Q2 pad 1: Net-(D2-Pad2) -> Net-(Q2-Pad1)
- Q2 pad 2: Net-(Q2-Pad2) -> Net-(D2-Pad1)
- Q2 pad 3: /Strand Select/MODR1 -> Net-(Q2-Pad3)
- Q20 pad 2: Net-(D22-Pad1) -> Net-(D22-Pad2)
- Q20 pad 3: /Strand Select/STR9 -> Net-(Q20-Pad3)
- Q21 pad 2: Net-(D23-Pad2) -> Net-(D23-Pad1)
- Q21 pad 3: /Strand Select/SE9 -> /Connector/STR9
- Q22 pad 2: Net-(D24-Pad1) -> Net-(D24-Pad2)
- Q22 pad 3: /Strand Select/STR10 -> Net-(Q22-Pad3)
- Q23 pad 2: Net-(D25-Pad2) -> Net-(D25-Pad1)
- Q23 pad 3: /Strand Select/SE10 -> /Connector/STR10
- Q24 pad 2: Net-(D26-Pad1) -> Net-(D26-Pad2)
- Q24 pad 3: /Strand Select/STR11 -> Net-(Q24-Pad3)
- Q25 pad 2: Net-(D27-Pad2) -> Net-(D27-Pad1)
- Q25 pad 3: /Strand Select/SE11 -> /Connector/STR11
- Q26 pad 2: Net-(D28-Pad1) -> Net-(D28-Pad2)
- Q26 pad 3: /Strand Select/STR12 -> Net-(Q26-Pad3)
- Q27 pad 2: Net-(D29-Pad2) -> Net-(D29-Pad1)
- Q27 pad 3: /Strand Select/SE12 -> /Connector/STR12
- Q29 pad 3: (no net) -> /Connector/XCN8
- Q3 pad 1: Net-(Q3-Pad1) -> Net-(D3-Pad2)
- Q3 pad 2: Net-(D5-Pad2) -> Net-(Q3-Pad2)
- Q3 pad 3: /Strand Select/RPR -> /Connector/MODR1
- Q31 pad 3: (no net) -> /Connector/XCN7
- Q33 pad 3: (no net) -> /Connector/XCN6
- Q35 pad 3: (no net) -> /Connector/XCN5
- Q37 pad 3: (no net) -> /Connector/XCN4
- Q39 pad 3: (no net) -> /Connector/XCN3
- Q4 pad 2: Net-(D6-Pad1) -> Net-(D6-Pad2)
- Q4 pad 3: /Strand Select/STR1 -> Net-(Q4-Pad3)
- Q41 pad 3: (no net) -> /Connector/XCN2
- Q43 pad 3: (no net) -> /Connector/XCN1
- Q45 pad 3: (no net) -> /Connector/XFN8
- Q47 pad 3: (no net) -> /Connector/XFN7
- Q49 pad 3: (no net) -> /Connector/XFN6
- Q5 pad 2: Net-(D7-Pad2) -> Net-(D7-Pad1)
- Q5 pad 3: /Strand Select/SE1 -> /Connector/STR1
- Q51 pad 3: (no net) -> /Connector/XFN5
- Q53 pad 3: (no net) -> /Connector/XFN4
- Q55 pad 3: (no net) -> /Connector/XFN3
- Q57 pad 3: (no net) -> /Connector/XFN2
- Q59 pad 3: (no net) -> /Connector/XFN1
- Q6 pad 2: Net-(D8-Pad1) -> Net-(D8-Pad2)
- Q6 pad 3: /Strand Select/STR2 -> Net-(Q6-Pad3)
- Q68 pad 3: /Rope Drivers/XRST4 -> /Connector/XRST4
- Q69 pad 3: /Rope Drivers/XRST4 -> /Connector/XRST4
- Q7 pad 2: Net-(D9-Pad2) -> Net-(D9-Pad1)
- Q7 pad 3: /Strand Select/SE2 -> /Connector/STR2
- Q72 pad 3: /Rope Drivers/XRST3 -> /Connector/XRST3
- Q73 pad 3: /Rope Drivers/XRST3 -> /Connector/XRST3
- Q76 pad 3: /Rope Drivers/XRST2 -> /Connector/XRST2
- Q77 pad 3: /Rope Drivers/XRST2 -> /Connector/XRST2
- Q8 pad 2: Net-(D10-Pad1) -> Net-(D10-Pad2)
- Q8 pad 3: /Strand Select/STR3 -> Net-(Q8-Pad3)
- Q80 pad 3: /Rope Drivers/XRST1 -> /Connector/XRST1
- Q81 pad 3: /Rope Drivers/XRST1 -> /Connector/XRST1
- Q84 pad 3: /Rope Drivers/XSET2 -> /Connector/XSET2
- Q85 pad 3: /Rope Drivers/XSET2 -> /Connector/XSET2
- Q88 pad 3: /Rope Drivers/XSET1 -> /Connector/XSET1
- Q89 pad 3: /Rope Drivers/XSET1 -> /Connector/XSET1
- Q9 pad 2: Net-(D11-Pad2) -> Net-(D11-Pad1)
- Q9 pad 3: /Strand Select/SE3 -> /Connector/STR3
- R10 pad 1: /Sense Amplifiers/BPLSWX -> GND
- R10 pad 2: (no net) -> Net-(R10-Pad2)
- R100 pad 1: /Strand Select/STR7 -> /Strand Select/BPLSWZ
- R100 pad 2: GND -> Net-(Q17-Pad1)
- R101 pad 2: /FPGA and Power/STEN7 -> Net-(Q16-Pad3)
- R102 pad 1: /Strand Select/BPLSWZ -> /Connector/STR7
- R102 pad 2: Net-(Q18-Pad1) -> GND
- R103 pad 2: /Strand Select/SE8 -> /FPGA and Power/SE8
- R104 pad 1: /Strand Select/STR8 -> /Strand Select/BPLSWZ
- R104 pad 2: GND -> Net-(Q19-Pad1)
- R105 pad 2: /FPGA and Power/STEN8 -> Net-(Q18-Pad3)
- R106 pad 1: /Strand Select/BPLSWZ -> /Connector/STR8
- R106 pad 2: Net-(Q20-Pad1) -> GND
- R107 pad 2: /Strand Select/SE9 -> /FPGA and Power/SE9
- R108 pad 1: /Strand Select/STR9 -> /Strand Select/BPLSWZ
- R108 pad 2: GND -> Net-(Q21-Pad1)
- R109 pad 2: /FPGA and Power/STEN9 -> Net-(Q20-Pad3)
- R11 pad 1: (no net) -> /Connector/GAR3
- R110 pad 1: /Strand Select/BPLSWZ -> /Connector/STR9
- R110 pad 2: Net-(Q22-Pad1) -> GND
- R111 pad 2: /Strand Select/SE10 -> /FPGA and Power/SE10
- R112 pad 1: /Strand Select/STR10 -> /Strand Select/BPLSWZ
- R112 pad 2: GND -> Net-(Q23-Pad1)
- R113 pad 2: /FPGA and Power/STEN10 -> Net-(Q22-Pad3)
- R114 pad 1: /Strand Select/BPLSWZ -> /Connector/STR10
- R114 pad 2: Net-(Q24-Pad1) -> GND
- R115 pad 2: /Strand Select/SE11 -> /FPGA and Power/SE11
- R116 pad 1: /Strand Select/STR11 -> /Strand Select/BPLSWZ
- R116 pad 2: GND -> Net-(Q25-Pad1)
- R117 pad 2: /FPGA and Power/STEN11 -> Net-(Q24-Pad3)
- R118 pad 1: /Strand Select/BPLSWZ -> /Connector/STR11
- R118 pad 2: Net-(Q26-Pad1) -> GND
- R119 pad 2: /Strand Select/SE12 -> /FPGA and Power/SE12
- R12 pad 2: (no net) -> /Connector/GBR3
- R120 pad 1: /Strand Select/STR12 -> /Strand Select/BPLSWZ
- R120 pad 2: GND -> Net-(Q27-Pad1)
- R121 pad 2: /FPGA and Power/STEN12 -> Net-(Q26-Pad3)
- R122 pad 1: Net-(Q28-Pad1) -> /Connector/STR12
- R122 pad 2: /FPGA and Power/~IL8 -> GND
- R123 pad 1: /Rope Drivers/40332A -> Net-(Q28-Pad1)
- R123 pad 2: Net-(D30-Pad2) -> /FPGA and Power/~IL8
- R124 pad 1: Net-(Q29-Pad2) -> /Rope Drivers/40332A
- R124 pad 2: (no net) -> Net-(D30-Pad2)
- R125 pad 1: Net-(Q30-Pad1) -> Net-(Q29-Pad2)
- R125 pad 2: /FPGA and Power/~IL7 -> Net-(R125-Pad2)
- R126 pad 1: /Rope Drivers/40332A -> Net-(R125-Pad2)
- R126 pad 2: Net-(D34-Pad2) -> Net-(L3-Pad1)
- R127 pad 1: Net-(Q31-Pad2) -> Net-(Q30-Pad1)
- R127 pad 2: (no net) -> /FPGA and Power/~IL7
- R128 pad 1: Net-(Q32-Pad1) -> /Rope Drivers/40332A
- R128 pad 2: /FPGA and Power/~IL6 -> Net-(D34-Pad2)
- R129 pad 1: /Rope Drivers/40332A -> Net-(Q31-Pad2)
- R129 pad 2: Net-(D38-Pad2) -> Net-(R129-Pad2)
- R13 pad 1: (no net) -> /Connector/GAR4
- R130 pad 1: Net-(Q33-Pad2) -> Net-(R129-Pad2)
- R130 pad 2: (no net) -> Net-(L4-Pad1)
- R131 pad 1: Net-(Q34-Pad1) -> Net-(Q32-Pad1)
- R131 pad 2: /FPGA and Power/~IL5 -> /FPGA and Power/~IL6
- R132 pad 2: Net-(D42-Pad2) -> Net-(D38-Pad2)
- R133 pad 1: Net-(Q35-Pad2) -> Net-(Q33-Pad2)
- R133 pad 2: (no net) -> Net-(R133-Pad2)
- R134 pad 1: Net-(Q36-Pad1) -> Net-(R133-Pad2)
- R134 pad 2: /FPGA and Power/~IL4 -> Net-(L5-Pad1)
- R135 pad 1: /Rope Drivers/40332A -> Net-(Q34-Pad1)
- R135 pad 2: Net-(D46-Pad2) -> /FPGA and Power/~IL5
- R136 pad 1: Net-(Q37-Pad2) -> /Rope Drivers/40332A
- R136 pad 2: (no net) -> Net-(D42-Pad2)
- R137 pad 1: Net-(Q38-Pad1) -> Net-(Q35-Pad2)
- R137 pad 2: /FPGA and Power/~IL3 -> Net-(R137-Pad2)
- R138 pad 1: /Rope Drivers/40331A -> Net-(R137-Pad2)
- R138 pad 2: Net-(D50-Pad2) -> Net-(L6-Pad1)
- R139 pad 1: Net-(Q39-Pad2) -> Net-(Q36-Pad1)
- R139 pad 2: (no net) -> /FPGA and Power/~IL4
- R14 pad 2: (no net) -> /Connector/GBR4
- R140 pad 1: Net-(Q40-Pad1) -> /Rope Drivers/40332A
- R140 pad 2: /FPGA and Power/~IL2 -> Net-(D46-Pad2)
- R141 pad 1: /Rope Drivers/40331A -> Net-(Q37-Pad2)
- R141 pad 2: Net-(D54-Pad2) -> Net-(R141-Pad2)
- R142 pad 1: Net-(Q41-Pad2) -> Net-(R141-Pad2)
- R142 pad 2: (no net) -> Net-(L7-Pad1)
- R143 pad 1: Net-(Q42-Pad1) -> Net-(Q38-Pad1)
- R143 pad 2: /FPGA and Power/~IL1 -> /FPGA and Power/~IL3
- R144 pad 2: Net-(D58-Pad2) -> Net-(D50-Pad2)
- R145 pad 1: Net-(Q43-Pad2) -> Net-(Q39-Pad2)
- R145 pad 2: (no net) -> Net-(R145-Pad2)
- R146 pad 1: Net-(Q44-Pad1) -> Net-(R145-Pad2)
- R146 pad 2: /FPGA and Power/IL8 -> Net-(L8-Pad1)
- R147 pad 1: /Rope Drivers/40331A -> Net-(Q40-Pad1)
- R147 pad 2: Net-(D62-Pad2) -> /FPGA and Power/~IL2
- R148 pad 1: Net-(Q45-Pad2) -> /Rope Drivers/40331A
- R148 pad 2: (no net) -> Net-(D54-Pad2)
- R149 pad 1: Net-(Q46-Pad1) -> Net-(Q41-Pad2)
- R149 pad 2: /FPGA and Power/IL7 -> Net-(R149-Pad2)
- R15 pad 1: (no net) -> Net-(R15-Pad1)
- R15 pad 2: /Sense Amplifiers/BPLSWX -> GND
- R150 pad 1: /Rope Drivers/40332A -> Net-(R149-Pad2)
- R150 pad 2: Net-(D66-Pad2) -> Net-(L9-Pad1)
- R151 pad 1: Net-(Q47-Pad2) -> Net-(Q42-Pad1)
- R151 pad 2: (no net) -> /FPGA and Power/~IL1
- R152 pad 1: Net-(Q48-Pad1) -> /Rope Drivers/40331A
- R152 pad 2: /FPGA and Power/IL6 -> Net-(D58-Pad2)
- R153 pad 1: /Rope Drivers/40332A -> Net-(Q43-Pad2)
- R153 pad 2: Net-(D70-Pad2) -> Net-(R153-Pad2)
- R154 pad 1: Net-(Q49-Pad2) -> Net-(R153-Pad2)
- R154 pad 2: (no net) -> Net-(L10-Pad1)
- R155 pad 1: Net-(Q50-Pad1) -> Net-(Q44-Pad1)
- R155 pad 2: /FPGA and Power/IL5 -> /FPGA and Power/IL8
- R156 pad 1: /Rope Drivers/40332A -> /Rope Drivers/40331A
- R156 pad 2: Net-(D74-Pad2) -> Net-(D62-Pad2)
- R157 pad 1: Net-(Q51-Pad2) -> Net-(Q45-Pad2)
- R157 pad 2: (no net) -> Net-(R157-Pad2)
- R158 pad 1: Net-(Q52-Pad1) -> Net-(R157-Pad2)
- R158 pad 2: /FPGA and Power/IL4 -> Net-(L11-Pad1)
- R159 pad 1: /Rope Drivers/40331A -> Net-(Q46-Pad1)
- R159 pad 2: Net-(D78-Pad2) -> /FPGA and Power/IL7
- R16 pad 1: /Sense Amplifiers/BPLSWX -> GND
- R16 pad 2: (no net) -> Net-(R16-Pad2)
- R160 pad 1: Net-(Q53-Pad2) -> /Rope Drivers/40332A
- R160 pad 2: (no net) -> Net-(D66-Pad2)
- R161 pad 1: Net-(Q54-Pad1) -> Net-(Q47-Pad2)
- R161 pad 2: /FPGA and Power/IL3 -> Net-(R161-Pad2)
- R162 pad 1: /Rope Drivers/40331A -> Net-(R161-Pad2)
- R162 pad 2: Net-(D82-Pad2) -> Net-(L12-Pad1)
- R163 pad 1: Net-(Q55-Pad2) -> Net-(Q48-Pad1)
- R163 pad 2: (no net) -> /FPGA and Power/IL6
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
